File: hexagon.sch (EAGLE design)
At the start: 27 parts, among them J1 AVR_SPI_PROG_3X22X3_LOCK, U1 ATMEGA328P_TQFP, Y2 16Mhz, Y2B 16MHz

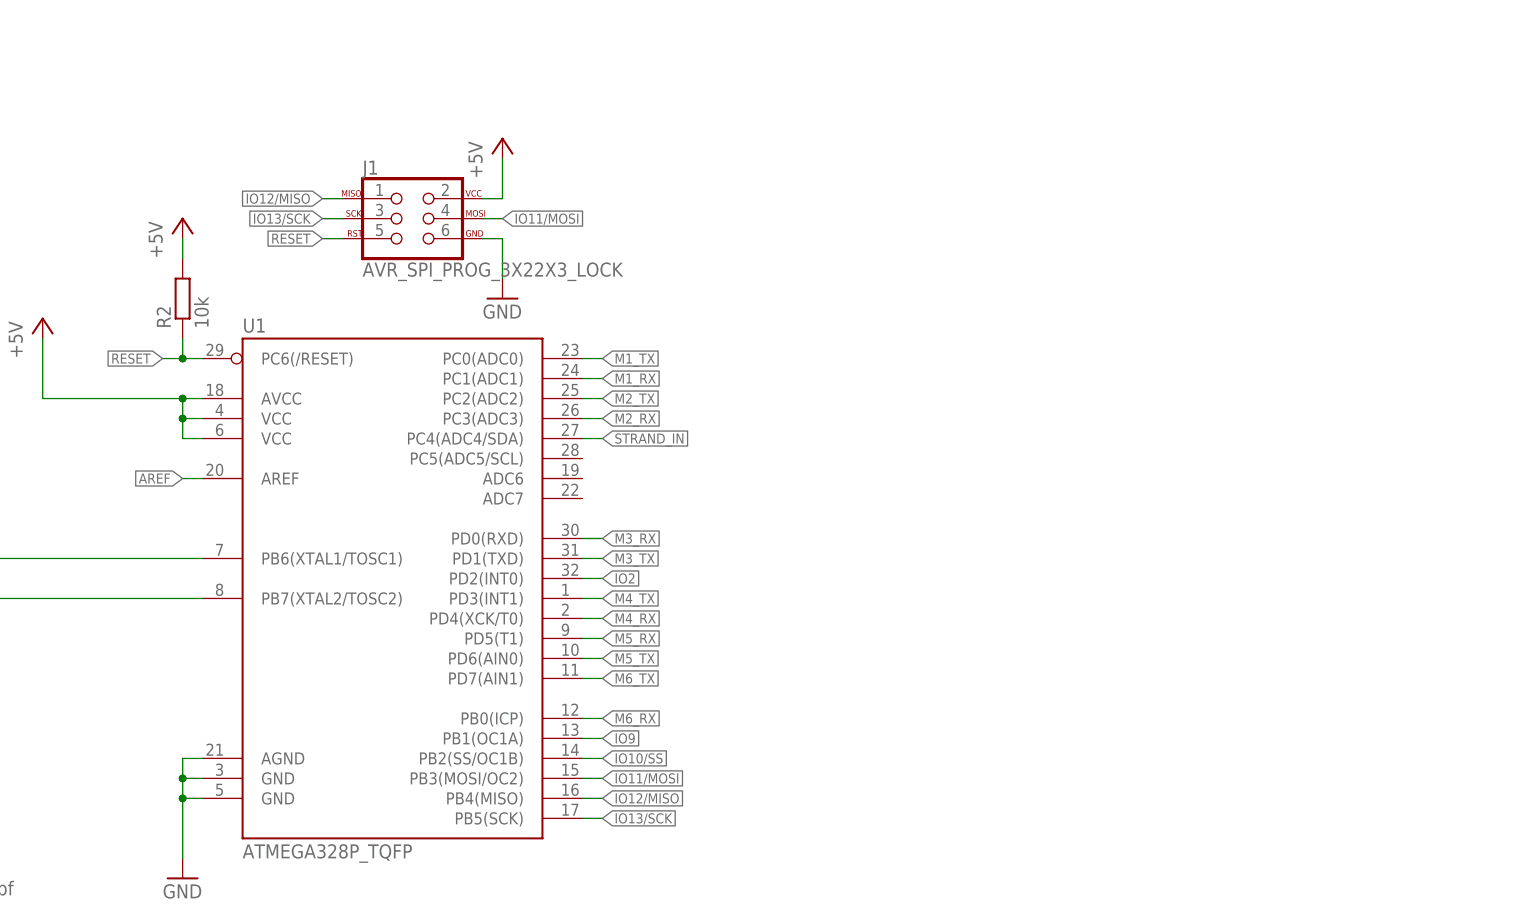
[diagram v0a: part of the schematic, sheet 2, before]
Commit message: Continuing to work out the layout kinks. Added ESP.
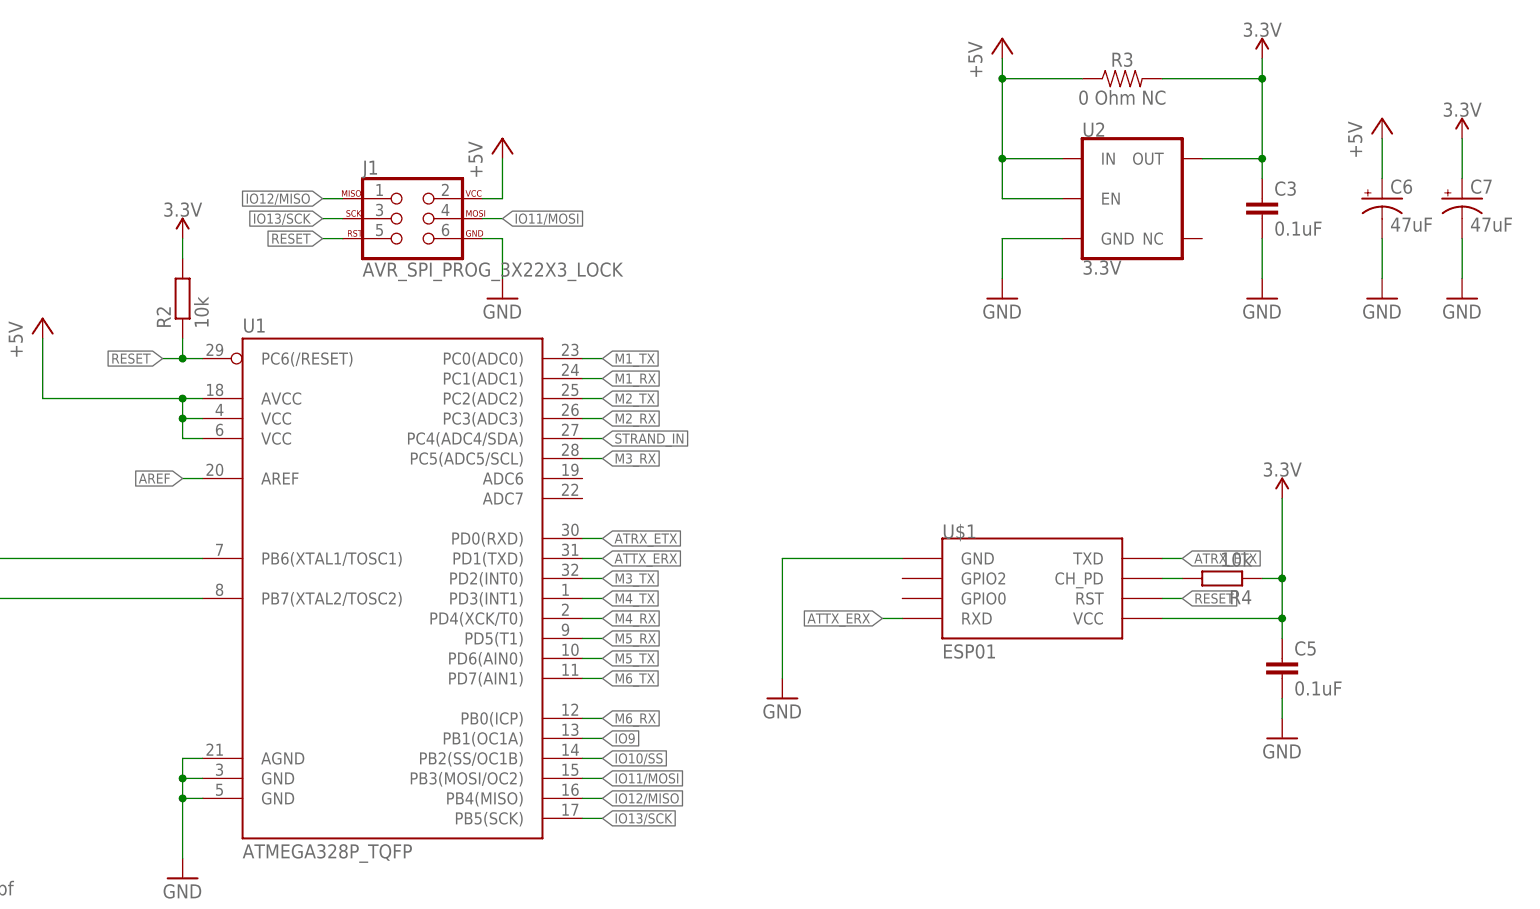
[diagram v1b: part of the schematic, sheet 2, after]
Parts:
- added C3, C5: 0.1uF, rcl:C-EUC0603
- added C6, C7: 47uF, SparkFun-Capacitors:47UF-POLAR-PANASONIC_D-35V-20%
- added R3: 0 Ohm NC, SparkFun-Resistors:RESISTOR0603
- added R4: 10k, rcl:R-EU_R0603
- added U$1: ESP01, esp8266modules:ESP01
- added U2: 3.3V, SparkFun-IC-Power:V_REG_AP2112K-3.3V
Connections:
- removed net IO2: U1.PD2(INT0)
- new net 3.3V: C3.1, C5.1, C7.+, R2.2, R3.2, R4.1, U$1.VCC, U2.OUT
- new net ATRX_ETX: U$1.TXD, U1.PD0(RXD)
- new net ATTX_ERX: U$1.RXD, U1.PD1(TXD)
- new net N$2: R4.2, U$1.CH_PD
- net +5V: now also C6.+, R3.1, U2.EN, U2.IN; no longer R2.2
- net GND: now also C3.2, C5.2, C6.-, C7.-, U$1.GND, U2.GND
- net M3_RX: now also U1.PC5(ADC5/SCL); no longer U1.PD0(RXD)
- net M3_TX: now also U1.PD2(INT0); no longer U1.PD1(TXD)
- net RESET: now also U$1.RST

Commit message: Gussy up with a readme and some renders
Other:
- moved on the sheet: C1, C2, C3, C4, C5, C6, C7, J1, M1, M2, M3, M4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
